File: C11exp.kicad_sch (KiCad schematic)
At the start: 29 parts, among them J2 UDPI, J9 Conn_01x06, Q1 IRLML2060, U9 ATmega4809-A

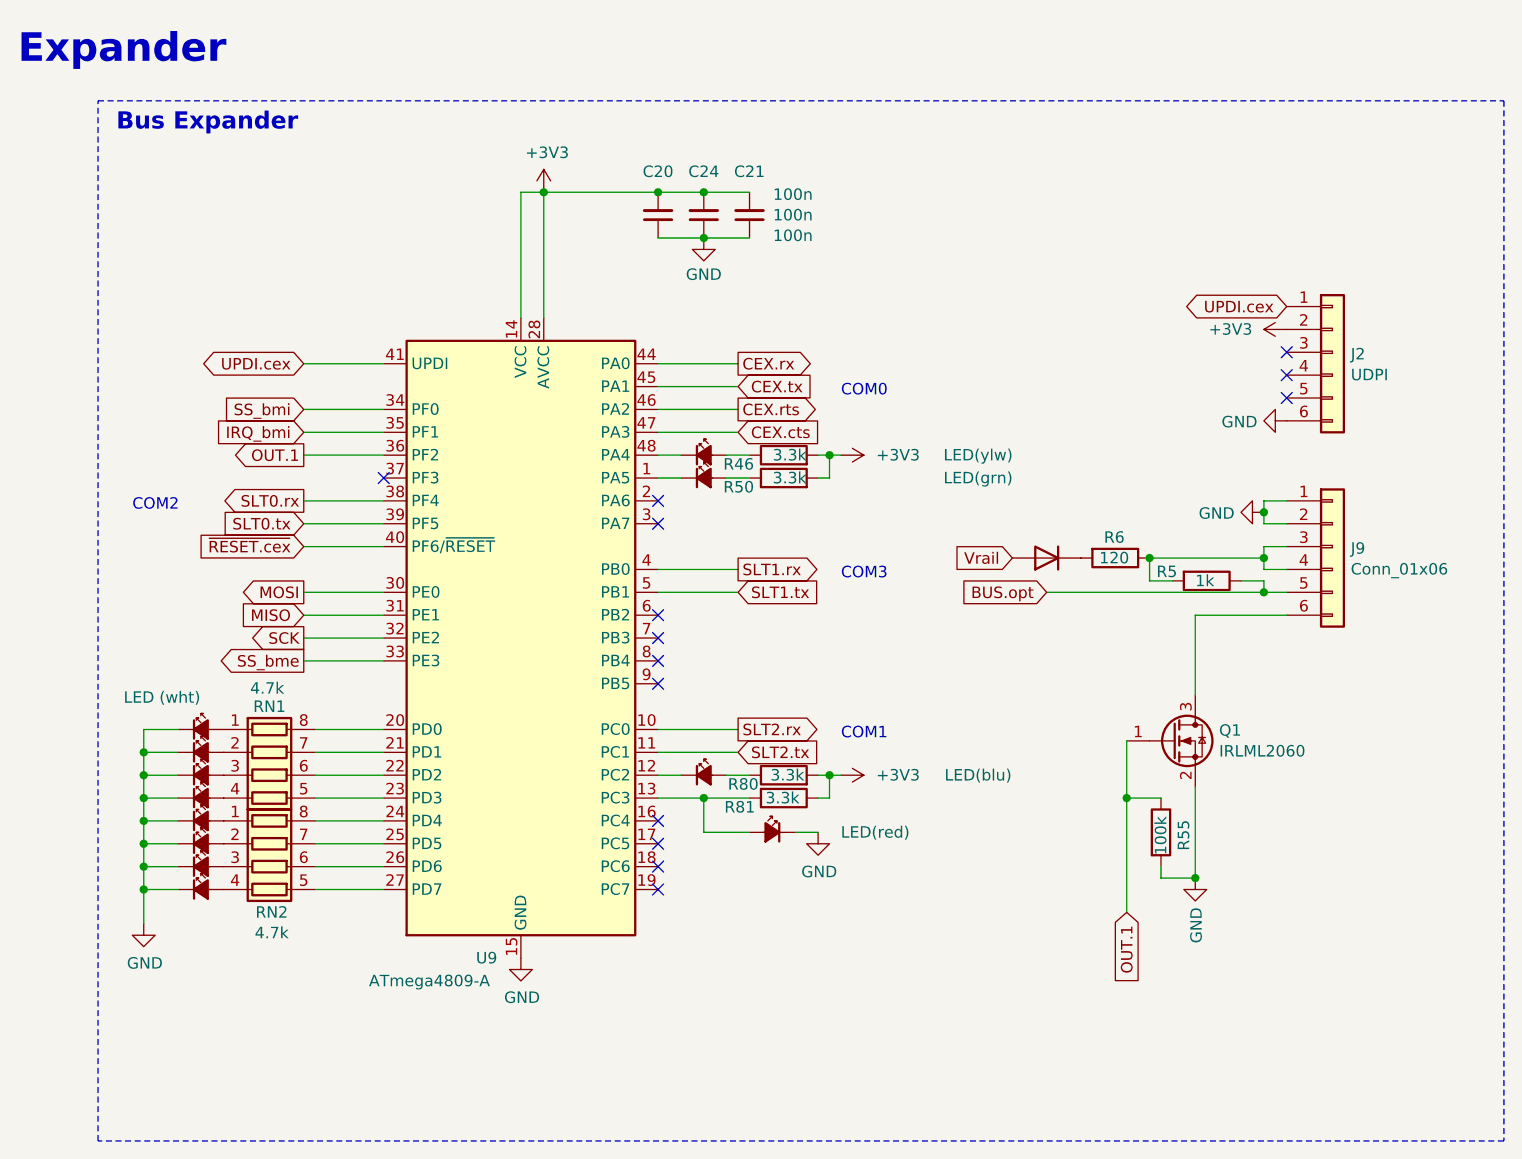
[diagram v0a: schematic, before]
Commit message: mod: changed to buck converter
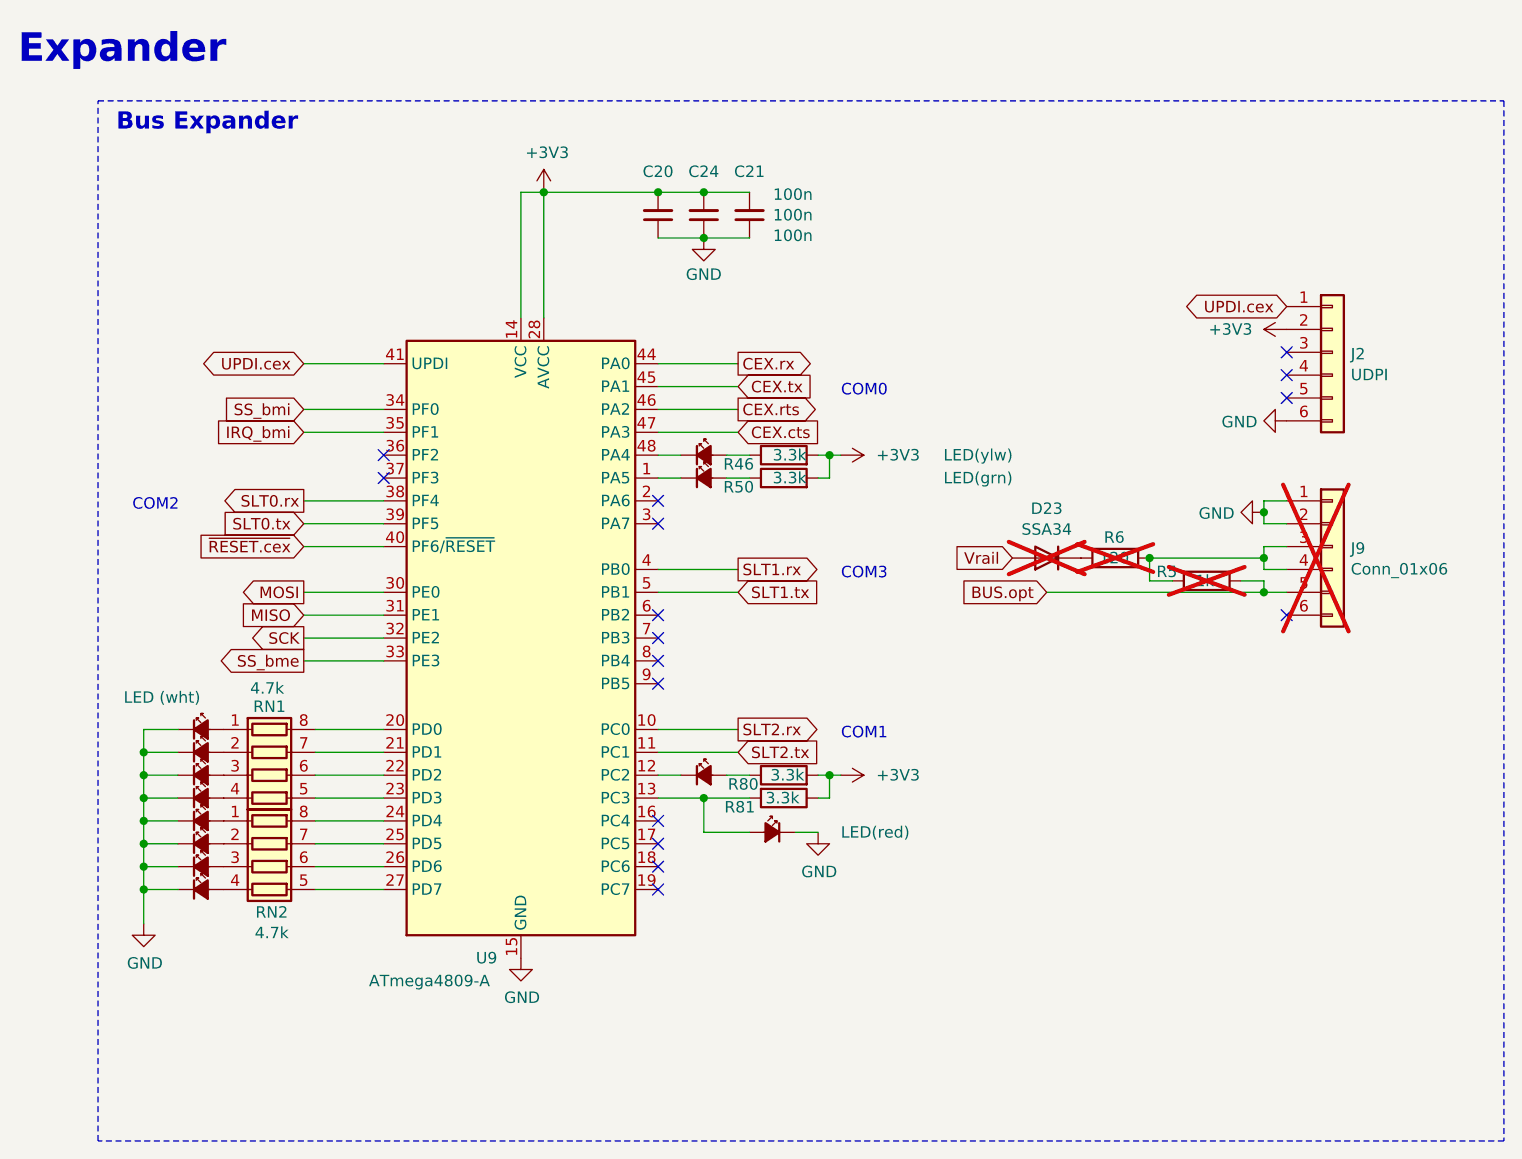
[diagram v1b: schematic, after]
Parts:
- removed Q1: IRLML2060, Package_TO_SOT_SMD:SOT-23, symbol Transistor_FET:IRLML2060
- removed R55: 100k, Resistor_SMD:R_0603_1608Metric, symbol Device:R
- C20: LCSC Part # (none) -> C49678
- C21, C24: LCSC Part # (none) -> C14663
- D10, D11, D12, D13, D15, D16, D17, D18, D19, D20, D21, D22, J2: now left out of the parts list
- D23: value D -> SSA34; LCSC Part # (none) -> C84632; now not fitted; now left out of the parts list
- J9: now not fitted; now left out of the parts list
- R46, R50, R80, R81: LCSC Part # (none) -> C22978
- R5: LCSC Part # (none) -> C4410; now not fitted; now left out of the parts list
- R6: LCSC Part # (none) -> C17909; now not fitted; now left out of the parts list
- RN1, RN2: LCSC Part # (none) -> C1980
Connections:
- net OUT.1: no longer names the net of U9.36 (PF2)
- no-connect marks 14 -> 16
